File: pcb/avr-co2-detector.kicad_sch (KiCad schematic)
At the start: 45 parts

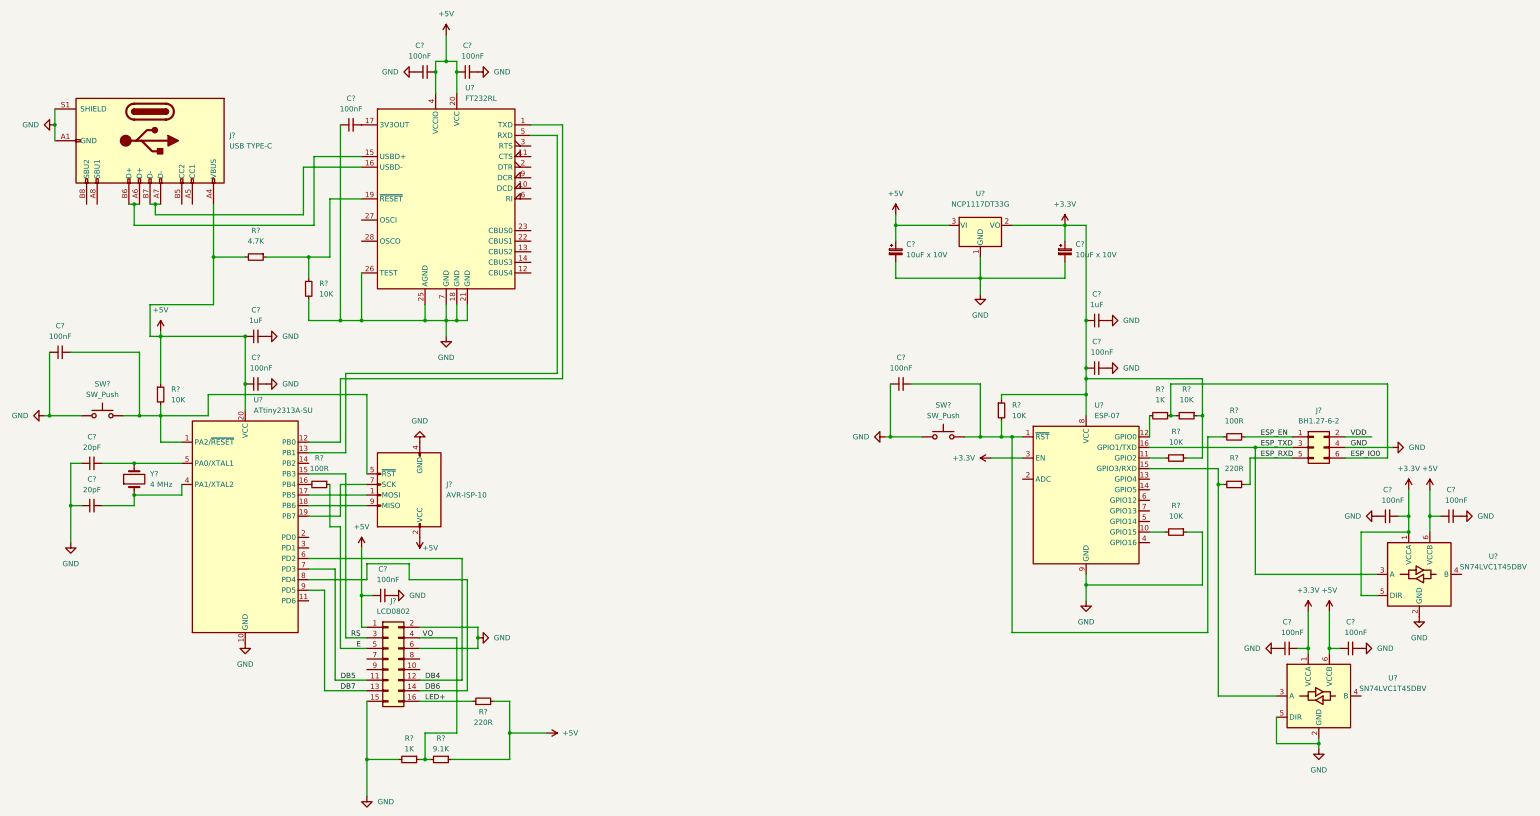
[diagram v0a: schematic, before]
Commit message: Added Senseair S8, connected ESP-07 UART to ATtiny2313A
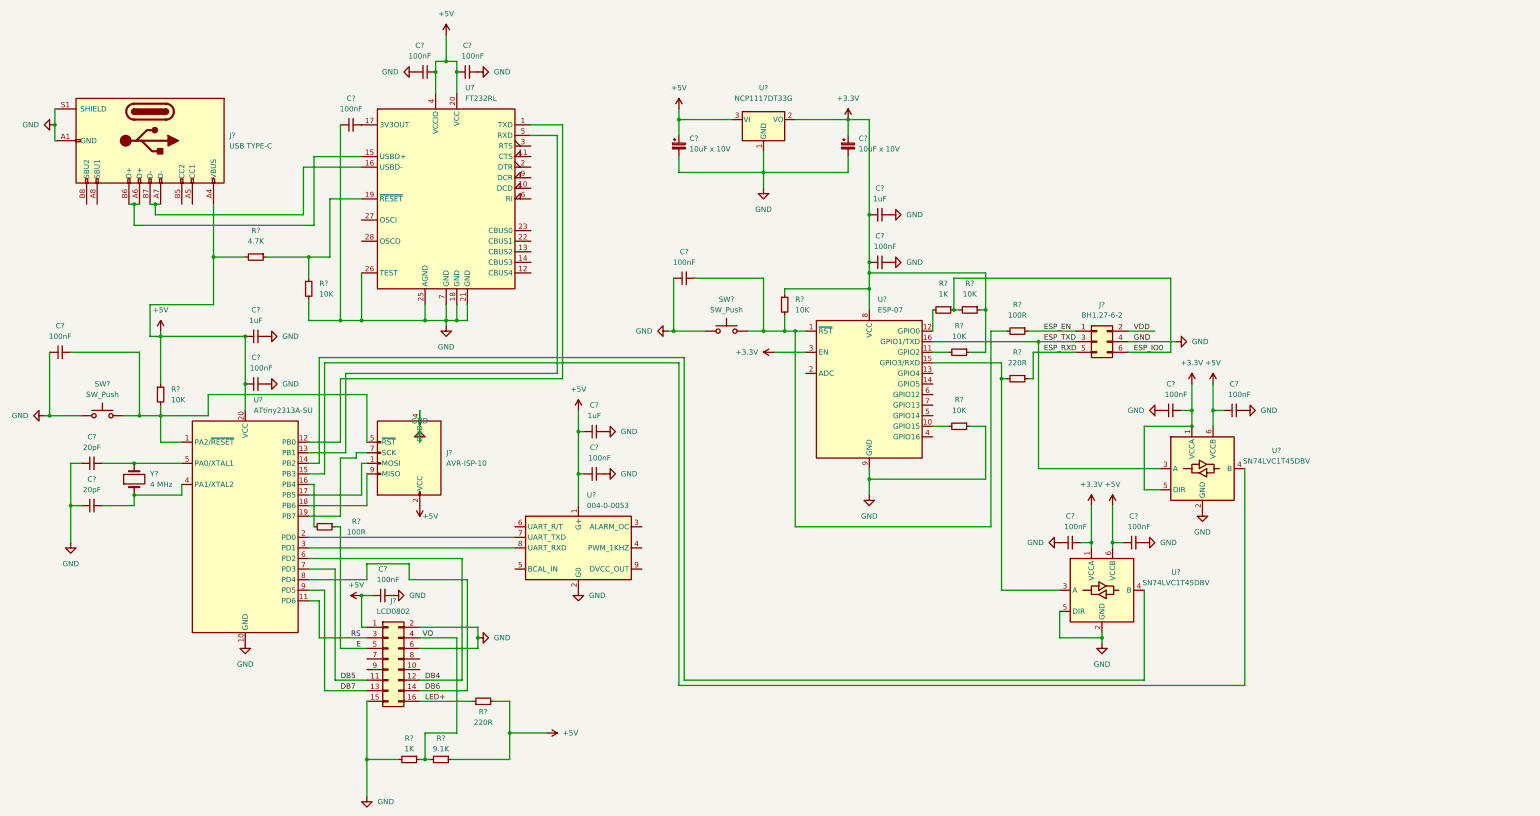
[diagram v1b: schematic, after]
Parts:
- added C?: 100nF, symbol Device:C_Small
- added C?: 1uF, symbol Device:C_Small
- added U?: 004-0-0053, symbol Sensor_Gas:004-0-0053
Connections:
- net +5V: now also C?.1, C?.1, U?.1 (G+)
- net GND: now also C?.2, C?.2, U?.2 (G0)
- net RS: now also U?.11 (PD6); no longer U?.15 (PB3)
- net at U?.4 (B): now also U?.15 (PB3)
- net at U?.14 (PB2): now also U?.4 (B)
- net at U?.2 (PD0): now also U?.7 (UART_TXD)
- net at U?.3 (PD1): now also U?.8 (UART_RXD)
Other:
- moved on the sheet: C?, J?, R?, SW?, U?

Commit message: Added configuration LED and button, debug UART RX jumper
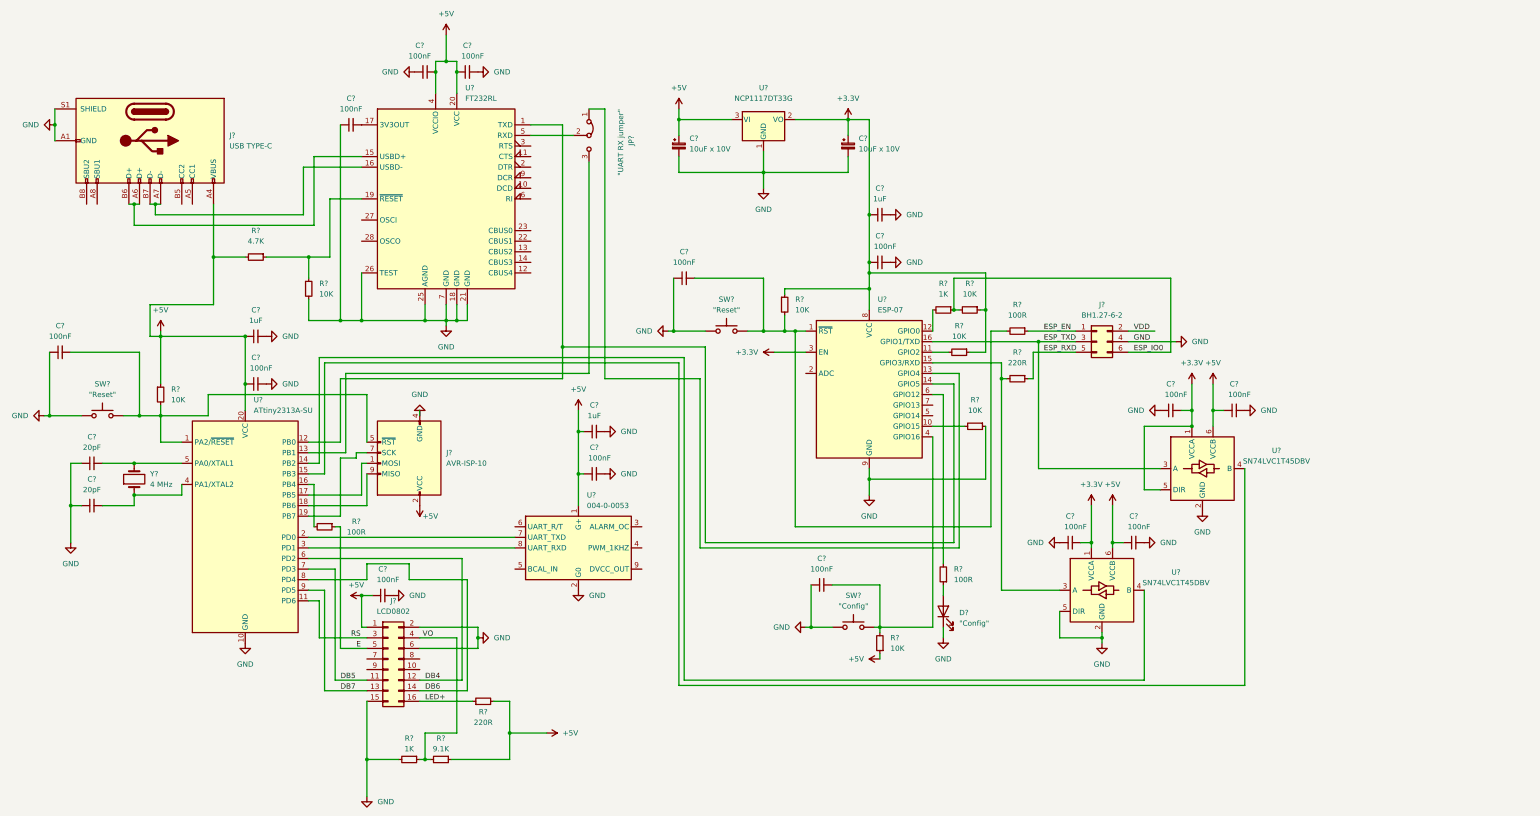
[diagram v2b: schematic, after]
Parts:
- added C?: 100nF, symbol Device:C_Small
- added D?: "Config", symbol Device:LED
- added JP?: "UART RX jumper", symbol Jumper:Jumper_3_Bridged12
- added R?: 100R, symbol Device:R_Small
- added R?: 10K, symbol Device:R_Small
- added SW?: "Config", symbol Switch:SW_Push
- SW? (x2): value SW_Push -> "Reset"
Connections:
- net +5V: now also R?.1
- net GND: now also C?.1, D?.1 (K), SW?.1
- net at U?.13 (GPIO4): now also JP?.1 (A)
- net at U?.14 (GPIO5): now also U?.1 (TXD), U?.12 (PB0)
- net at U?.4 (GPIO16): now also C?.2, R?.2, SW?.2
- net at U?.6 (GPIO12): now also R?.2
- net at U?.5 (RXD): now also JP?.2 (C); no longer U?.13 (PB1)
- new net: D?.2 (A), R?.1
- new net: JP?.3 (B), U?.13 (PB1)
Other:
- moved on the sheet: R?

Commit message: Added level shifters for ESP-07 debug UART
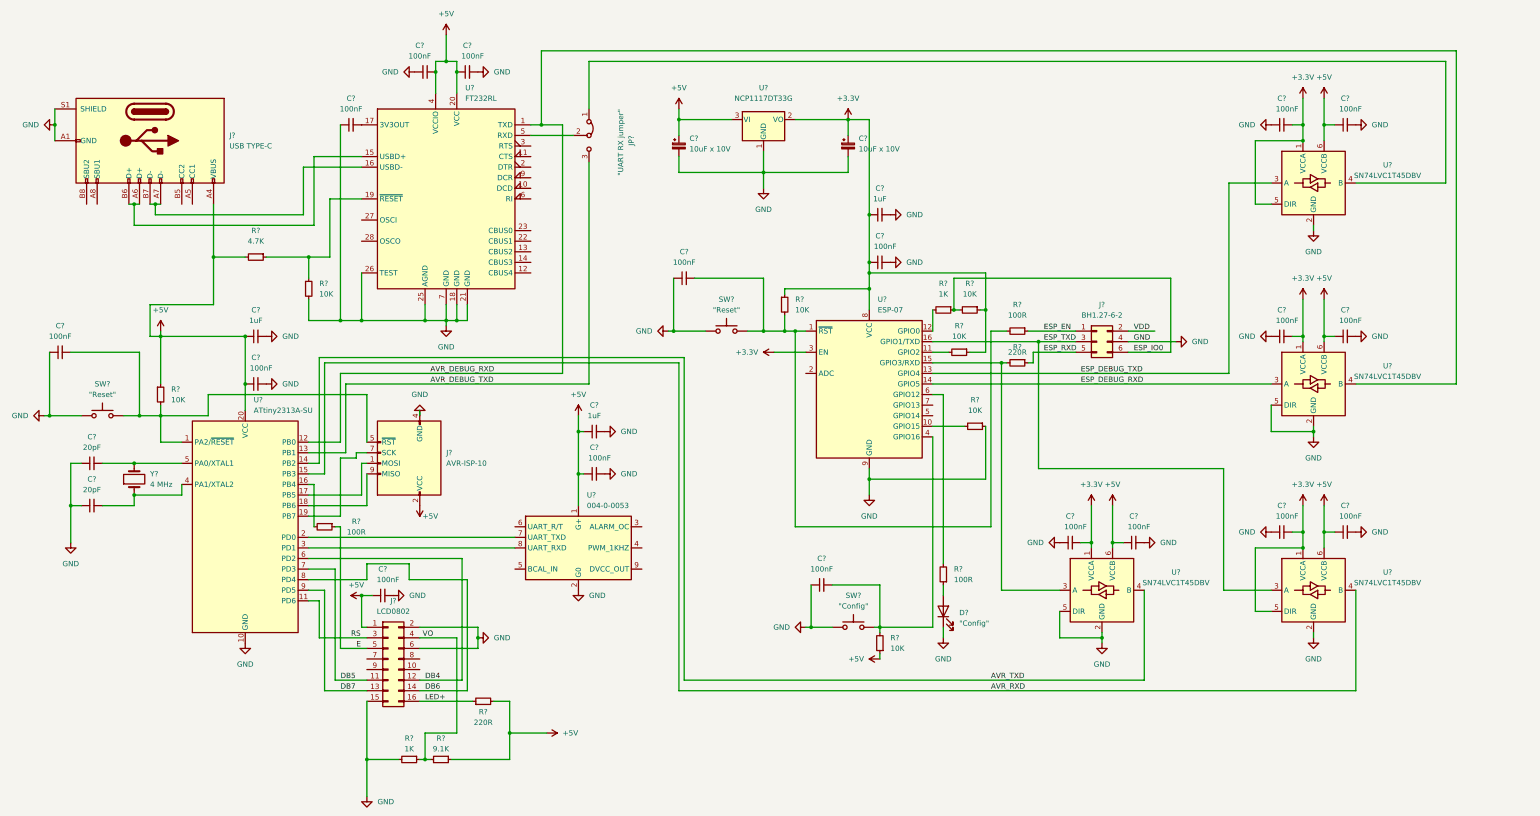
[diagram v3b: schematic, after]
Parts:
- added C? (x4): 100nF, symbol Device:C_Small
- added U? (x2): SN74LVC1T45DBV, Package_TO_SOT_SMD:SOT-23-6, symbol Logic_LevelTranslator:SN74LVC1T45DBV
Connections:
- net +3.3V: now also C?.2, C?.2, U?.1 (VCCA), U?.1 (VCCA), U?.5 (DIR)
- net +5V: now also C?.1, C?.1, U?.6 (VCCB), U?.6 (VCCB)
- net GND: now also C?.1, C?.1, C?.2, C?.2, U?.2 (GND), U?.2 (GND), U?.5 (DIR)
- net at JP?.1 (A): now also U?.4 (B); no longer U?.13 (GPIO4)
- net AVR_DEBUG_RXD: now reaches U?.1 (TXD), U?.12 (PB0)
- net AVR_DEBUG_RXD: now also U?.4 (B); no longer U?.14 (GPIO5)
- net AVR_RXD: now reaches U?.15 (PB3), U?.4 (B)
- net AVR_DEBUG_TXD: now reaches JP?.3 (B), U?.13 (PB1)
- net AVR_TXD: now reaches U?.14 (PB2), U?.4 (B)
- new net ESP_DEBUG_RXD: U?.14 (GPIO5), U?.3 (A)
- new net ESP_DEBUG_TXD: U?.13 (GPIO4), U?.3 (A)
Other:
- moved on the sheet: C?, R?, U?

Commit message: Annotated all parts, assigned all footprints, exported to pcb
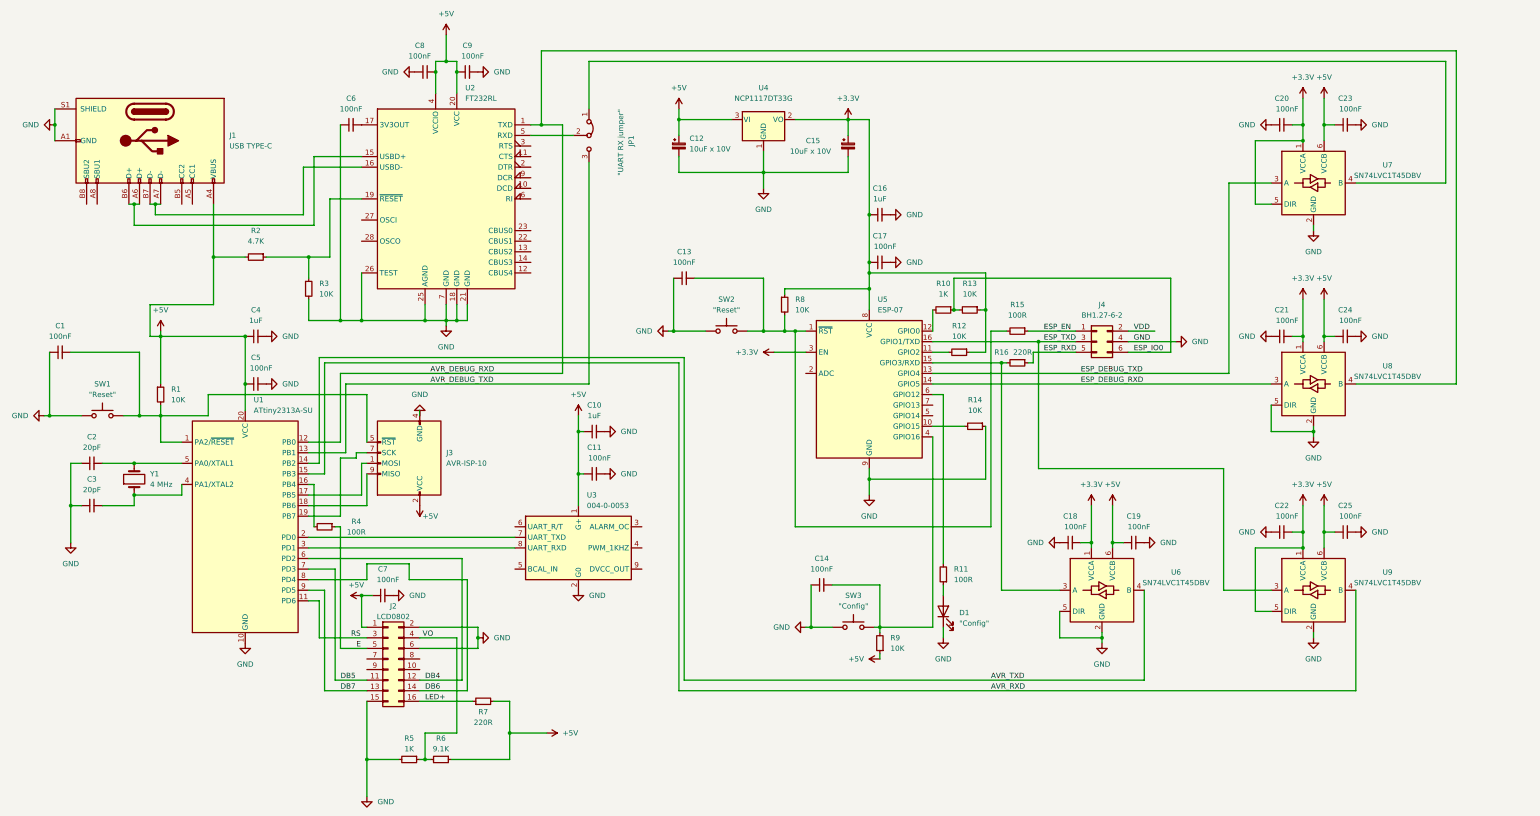
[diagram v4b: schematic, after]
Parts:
- C1, C10, C11, C13, C14, C16, C17, C18, C19, C2, C20, C21, C22, C23, C24, C25, C3, C4, C5, C6, C7, C8, C9: renamed from C?; footprint (none) -> Capacitor_SMD:C_0805_2012Metric_Pad1.18x1.45mm_HandSolder
- C12, C15: renamed from C?; footprint (none) -> Capacitor_Tantalum_SMD:CP_EIA-3216-18_Kemet-A_Pad1.58x1.35mm_HandSolder
- D1: renamed from D?; footprint (none) -> LED_THT:LED_D3.0mm_FlatTop
- J2: renamed from J?; footprint (none) -> Connector_IDC:IDC-Header_2x08_P2.54mm_Vertical
- J3: renamed from J?; footprint (none) -> Connector_IDC:IDC-Header_2x05_P2.54mm_Vertical
- J4: renamed from J?; footprint (none) -> Connector:Tag-Connect_TC2030-IDC-NL_2x03_P1.27mm_Vertical
- JP1: renamed from JP?; footprint (none) -> Connector_PinHeader_2.54mm:PinHeader_1x03_P2.54mm_Vertical
- R1, R10, R11, R12, R13, R14, R15, R16, R2, R3, R4, R5, R6, R7, R8, R9: renamed from R?; footprint (none) -> Resistor_SMD:R_0805_2012Metric_Pad1.20x1.40mm_HandSolder
- SW1, SW2, SW3: renamed from SW?; footprint (none) -> Button_Switch_SMD:SW_Push_1P1T_NO_6x6mm_H9.5mm
- U3: renamed from U?; footprint (none) -> Sensor:Senseair_S8_Up
- Y1: renamed from Y?; footprint (none) -> Crystal:Crystal_SMD_HC49-SD
- gave numbers to parts that had none: 9
